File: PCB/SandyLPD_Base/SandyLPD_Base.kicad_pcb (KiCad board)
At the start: 2 copper layers, 271.5 x 101 mm, 244 parts, among them J1 Conn_02x02_Odd_Even, J10 Conn_01x10_Pin, J11 Conn_01x03, J2 Conn_01x03, J4 Conn_01x10_Pin, J5 USB_C_Receptacle_USB2.0, J6 USB_C_Receptacle_USB2.0, J7 USB_C_Receptacle_USB2.0, J8 USB_C_Receptacle_USB2.0, J9 Conn_02x02_Odd_Even, SW1 BOOT_ALT, SW2 RESET_ALT, SW3 SW_DIP_x04, SW4 BOOT_ALT, SW5 RESET_ALT, SW6 SW_DIP_x04, U1 NCP1117-3.3_SOT223, U2 NCP1117-3.3_SOT223, U3 RP2040, U4 W25Q128JVPIQ, U5 RP2040, U6 W25Q128JVPIQ, Y1 12MHz, Y2 12MHz

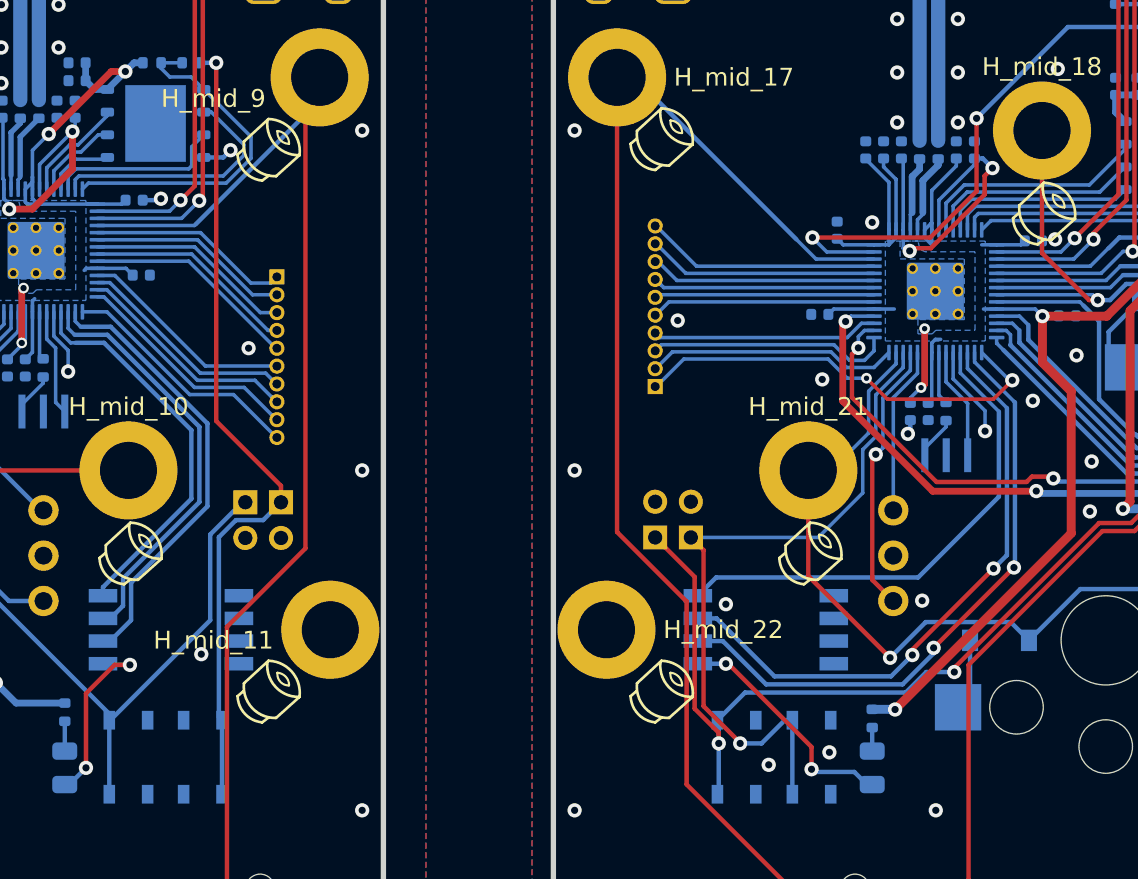
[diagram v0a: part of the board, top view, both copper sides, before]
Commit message: DIPスイッチ取り付け前に通電確認できるジャンパを追加。 #42
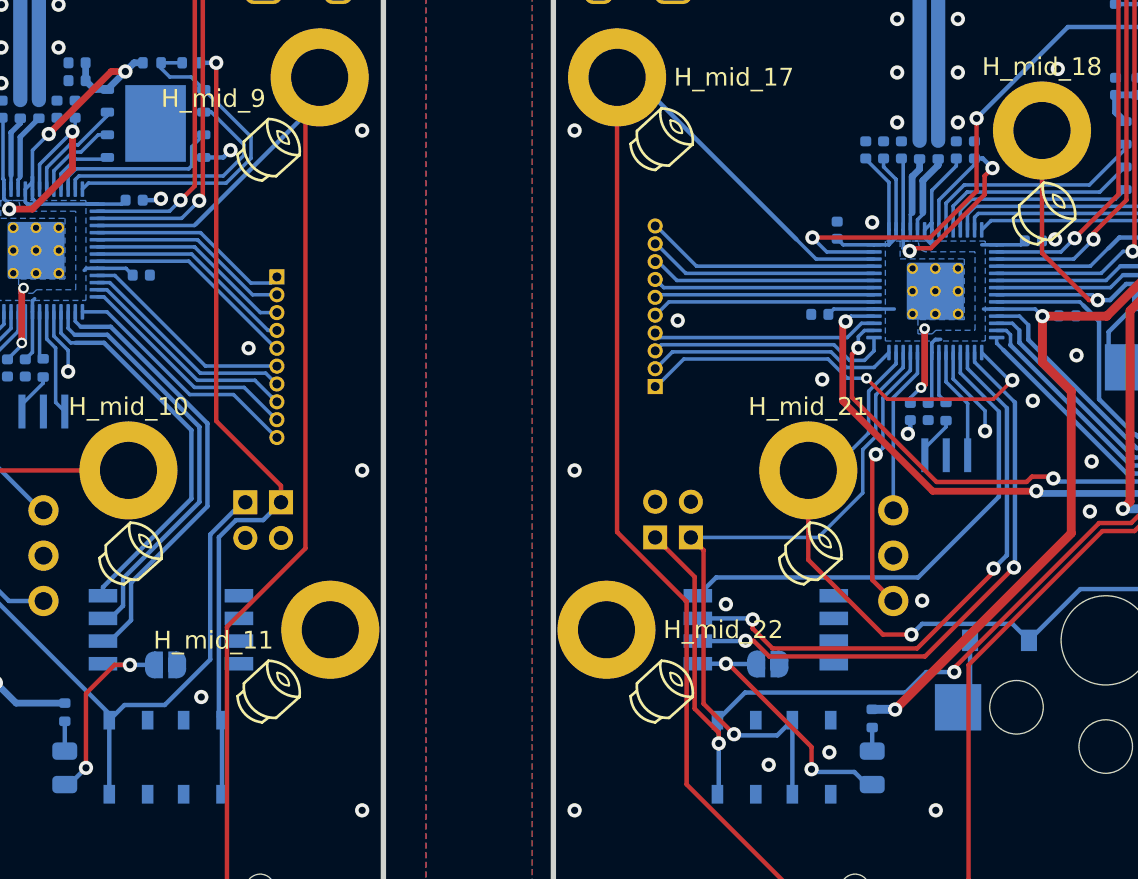
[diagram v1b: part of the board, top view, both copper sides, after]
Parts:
- added JP1: SolderJumper_2_Open, locallib:SolderJumper-2_P1.3mm_Open_RoundedPad1.0x1.5mm_no_Courtyard, B.Cu at (142.2, 85.5)
- added JP3: SolderJumper_2_Open, locallib:SolderJumper-2_P1.3mm_Open_RoundedPad1.0x1.5mm_no_Courtyard, B.Cu at (176.0, 85.5)
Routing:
- net PowerLED_R: track 13.3 -> 15.0 mm
- net R_row2: track 129.8 -> 128.1 mm
- net R_dip3: track 35.0 -> 33.6 mm
- net PowerLED_L: track 10.8 -> 12.2 mm
- net L_RESET: track 46.3 -> 47.6 mm
- net R_dip2: track 34.3 -> 33.2 mm

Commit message: 配線調整
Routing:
- net R_row3: track 148.5 -> 147.1 mm
- net Net-(D20-A): track 4.93 -> 5.51 mm

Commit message: シルク調整
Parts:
- H_btm_1, H_btm_2, H_btm_3, H_btm_4, H_btm_5, H_btm_6: footprint locallib:MountingHole_M2_Through-hole_tap_THC-0.8-1.0-2 -> locallib:MountingHole_M2_Through-hole_tap_THC-0.8-1.0-2_minimal
- H_mid_1, H_mid_10, H_mid_11, H_mid_12, H_mid_13, H_mid_14, H_mid_15, H_mid_16, H_mid_17, H_mid_18, H_mid_19, H_mid_2, H_mid_20, H_mid_21, H_mid_22, H_mid_3, H_mid_4, H_mid_5, H_mid_6, H_mid_7, H_mid_8, H_mid_9: footprint locallib:MountingHole_M2_Through-hole_tap_THC-0.8-2.0-2 -> locallib:MountingHole_M2_Through-hole_tap_THC-0.8-2.0-2_minimal
- moved REF** 9.24 mm to (237.8, 76.4)
- moved REF** 5.86 mm to (146.7, 112.7)
- moved REF** 2.64 mm to (172.3, 37.1)
- moved REF** 1.88 mm to (80.0, 77.6)
- moved REF** 1.88 mm to (289.5, 109.8)
- moved REF** 1.35 mm to (145.4, 37.2)
- moved REF** 0.84 mm to (171.7, 112.1)
